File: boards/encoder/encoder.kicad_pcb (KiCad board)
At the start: 4 copper layers, 50 x 40 mm, 87 parts, among them IC1 TPT480, J1 SWD, J2 Sensore, J3 Sensore, J4 CANbus, J5 RS485, J6 PWR, Q1 Q_PMOS_GSD, SW1 SW_SPST, SW2 SW_SPST, SW3 SW_Push, SW4 204_211ST, U1 MSPM0G310x, U10 TPS62A02A, U2 M24C08, U3 CT310, U4 INA826, U5 INA826, U6 LMR342FVJ, U7 QSZ2TR, U8 AZ431-A, U9 TCAN1044V

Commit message: v1.0.1
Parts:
- moved R2 0.25 mm to (139.4, 102.8)
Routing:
- net VDDA: track 49.6 -> 54.4 mm, vias 6 -> 5
- net VDD: track 112.8 -> 115.8 mm
- net GND: track 48.3 -> 50.0 mm
- net /VBIAS: track 19.7 -> 20.8 mm
- net GNDA: track 25.7 -> 26.6 mm

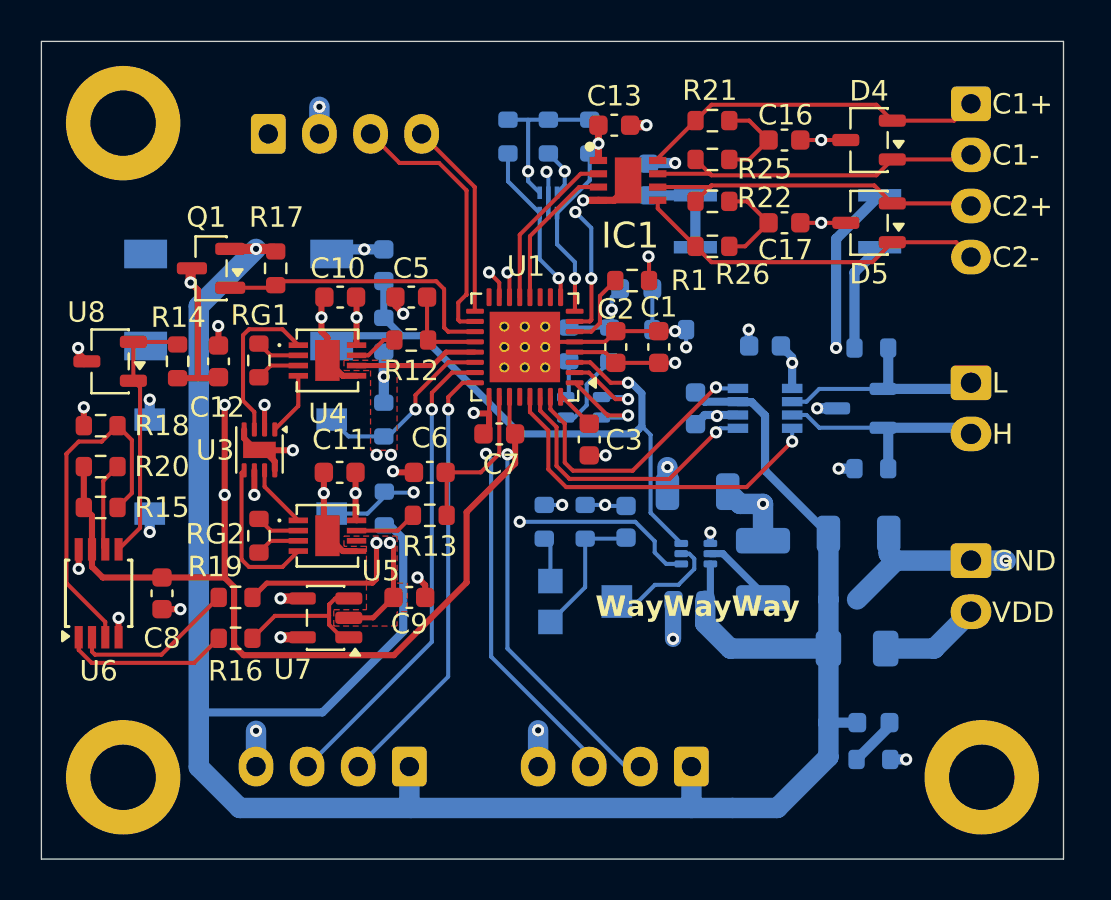
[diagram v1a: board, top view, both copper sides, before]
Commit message: Fixed ERC errors
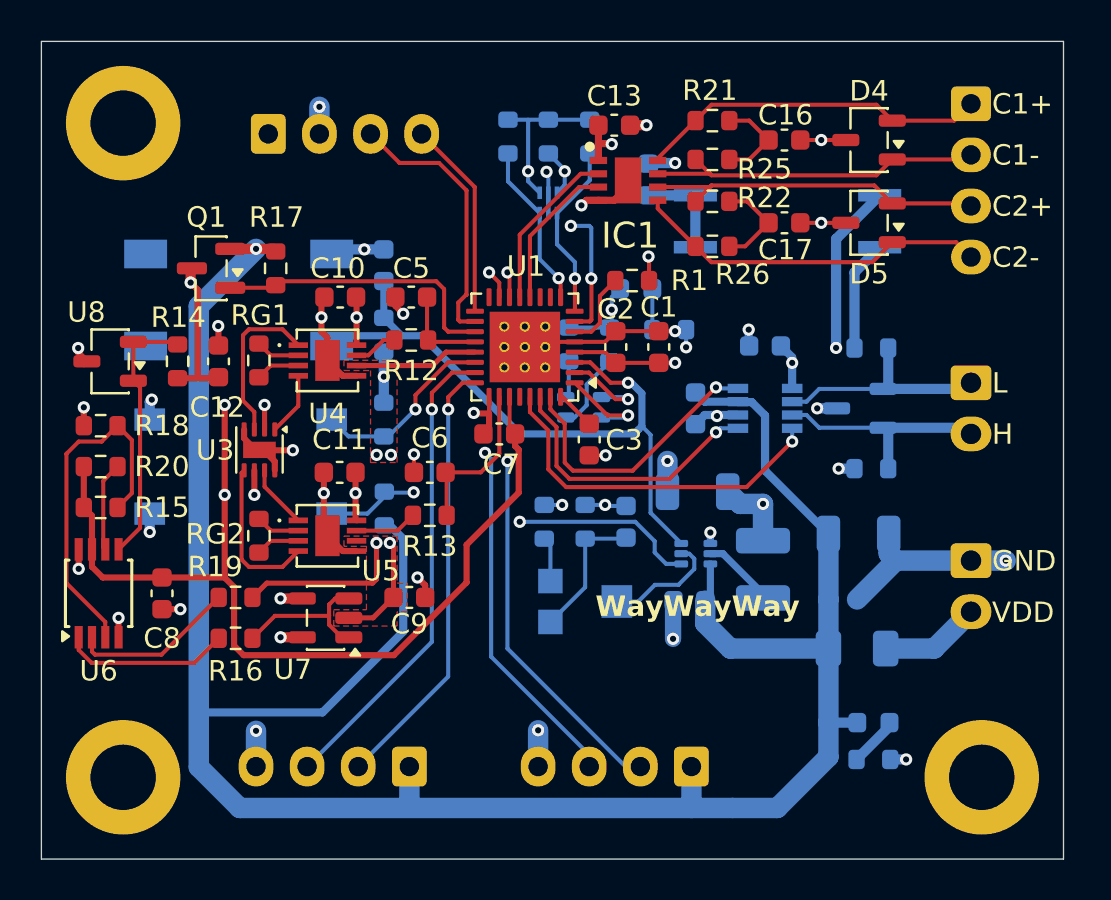
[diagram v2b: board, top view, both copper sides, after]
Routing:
- net GND: track 50.0 -> 50.5 mm
- net /I2C_SDA: track 11.1 -> 11.6 mm
- net /VBIAS: track 20.8 -> 20.3 mm

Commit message: v1.0.2
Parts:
- C4: value 20n -> 22n
- D3: value HT-264USD/UYG-5522 -> MCU
- R14: value 100 -> 1k
- R21, R22, R23, R24, R25, R26: value 60 -> 60.4
- R5, R6: value 150 -> 261
- R7: renamed from R8; value 150 -> 261
- R8: renamed from R7; value 348 -> 590
- U10: footprint Package_TO_SOT_SMD:SOT-563 -> metis-vela:SOT6_DRL_TEX
